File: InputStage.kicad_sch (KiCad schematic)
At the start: 19 parts, among them SW1 218-8LPSTR, SW44 SW_DIP_x02, SW50 SW_DPDT_x2, SW53 CS-4-14, U15 OPA992DBV

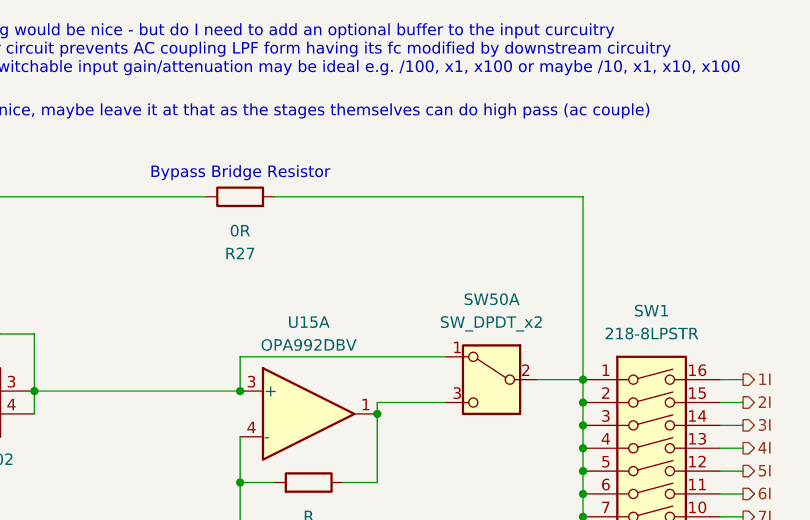
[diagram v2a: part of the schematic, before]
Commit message: Input and output routing complete
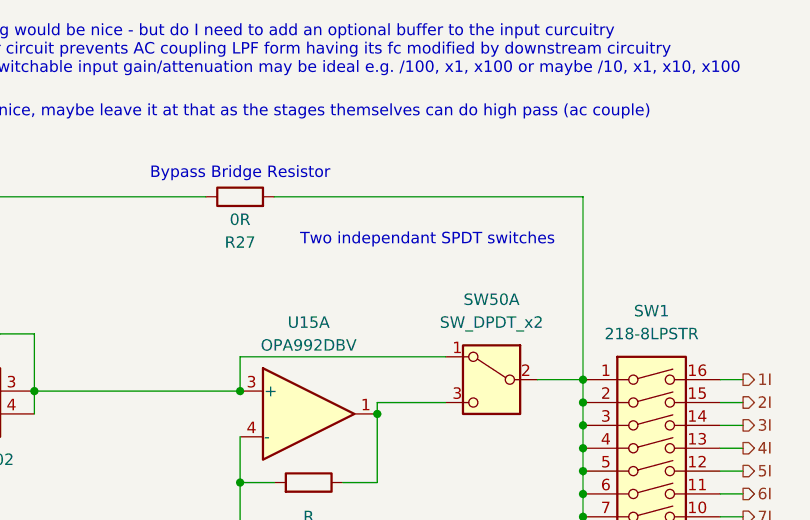
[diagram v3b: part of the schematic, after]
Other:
- note added: "Two independant SPDT switches"
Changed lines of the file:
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@@
+		)
+	)
+	(text "Two independant SPDT switches"
+		(exclude_from_sim no)
+		(at 119.888 49.276 0)
+		(effects
+			(font
+				(size 1.27 1.27)
+			)
 		)
 	)
@@
 		(dnp no)
 		(property "Reference" "R27"
-			(at 99.06 50.8 90)
+			(at 99.06 49.53 90)
 			(show_name no)
 			(do_not_autoplace no)
@@
 		)
 		(property "Value" "0R"
-			(at 99.06 48.26 90)
-			(show_name no)
-			(do_not_autoplace no)
+			(at 99.06 46.99 90)
+			(show_name no)
+			(do_not_autoplace no)
